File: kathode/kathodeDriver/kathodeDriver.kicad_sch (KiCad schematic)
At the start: 226 parts, among them J1 Conn_01x04, J2 Conn_01x02, Q1 Q_NPN_BEC, Q10 Q_NPN_BEC, Q11 Q_NPN_BEC, Q12 Q_NPN_BEC, Q13 Q_NPN_BEC, Q14 Q_NPN_BEC, Q15 Q_NPN_BEC, Q16 Q_NPN_BEC, Q17 Q_NPN_BEC, Q18 Q_NPN_BEC, Q19 Q_NPN_BEC, Q2 Q_NPN_BEC, Q20 Q_NPN_BEC, Q21 Q_NPN_BEC, Q22 Q_NPN_BEC, Q23 Q_NPN_BEC, Q24 Q_NPN_BEC, Q25 Q_NPN_BEC, Q26 Q_NPN_BEC, Q27 Q_NPN_BEC, Q28 Q_NPN_BEC, Q29 Q_NPN_BEC, Q3 Q_NPN_BEC, Q30 Q_NPN_BEC, Q31 Q_NPN_BEC, Q32 Q_NPN_BEC, Q33 Q_NPN_BEC, Q34 Q_NPN_BEC, Q35 Q_NPN_BEC, Q36 Q_NPN_BEC, Q37 Q_NPN_BEC, Q38 Q_NPN_BEC, Q39 Q_NPN_BEC, Q4 Q_NPN_BEC, Q40 Q_NPN_BEC, Q41 Q_NPN_BEC, Q42 Q_NPN_BEC, Q43 Q_NPN_BEC, Q44 Q_NPN_BEC, Q45 Q_NPN_BEC, Q46 Q_NPN_BEC, Q47 Q_NPN_BEC, Q48 Q_NPN_BEC, Q49 Q_NPN_BEC, Q5 Q_NPN_BEC, Q50 Q_NPN_BEC, Q51 Q_NPN_BEC, Q52 Q_NPN_BEC, Q53 Q_NPN_BEC, Q54 Q_NPN_BEC, Q55 Q_NPN_BEC, Q56 Q_NPN_BEC, Q57 Q_NPN_BEC, Q58 Q_NPN_BEC, Q59 Q_NPN_BEC, Q6 Q_NPN_BEC, Q60 Q_NPN_BEC, Q61 Q_NPN_BEC, Q62 Q_NPN_BEC, Q63 Q_NPN_BEC, Q64 Q_NPN_BEC, Q7 Q_NPN_BEC, Q8 Q_NPN_BEC, Q9 Q_NPN_BEC, U1 74AUP1G32, U10 4017, U11 4017, U2 4017, U3 4081, U4 4081, U5 4017, U6 4017, U7 4017, U8 4017, U9 4017

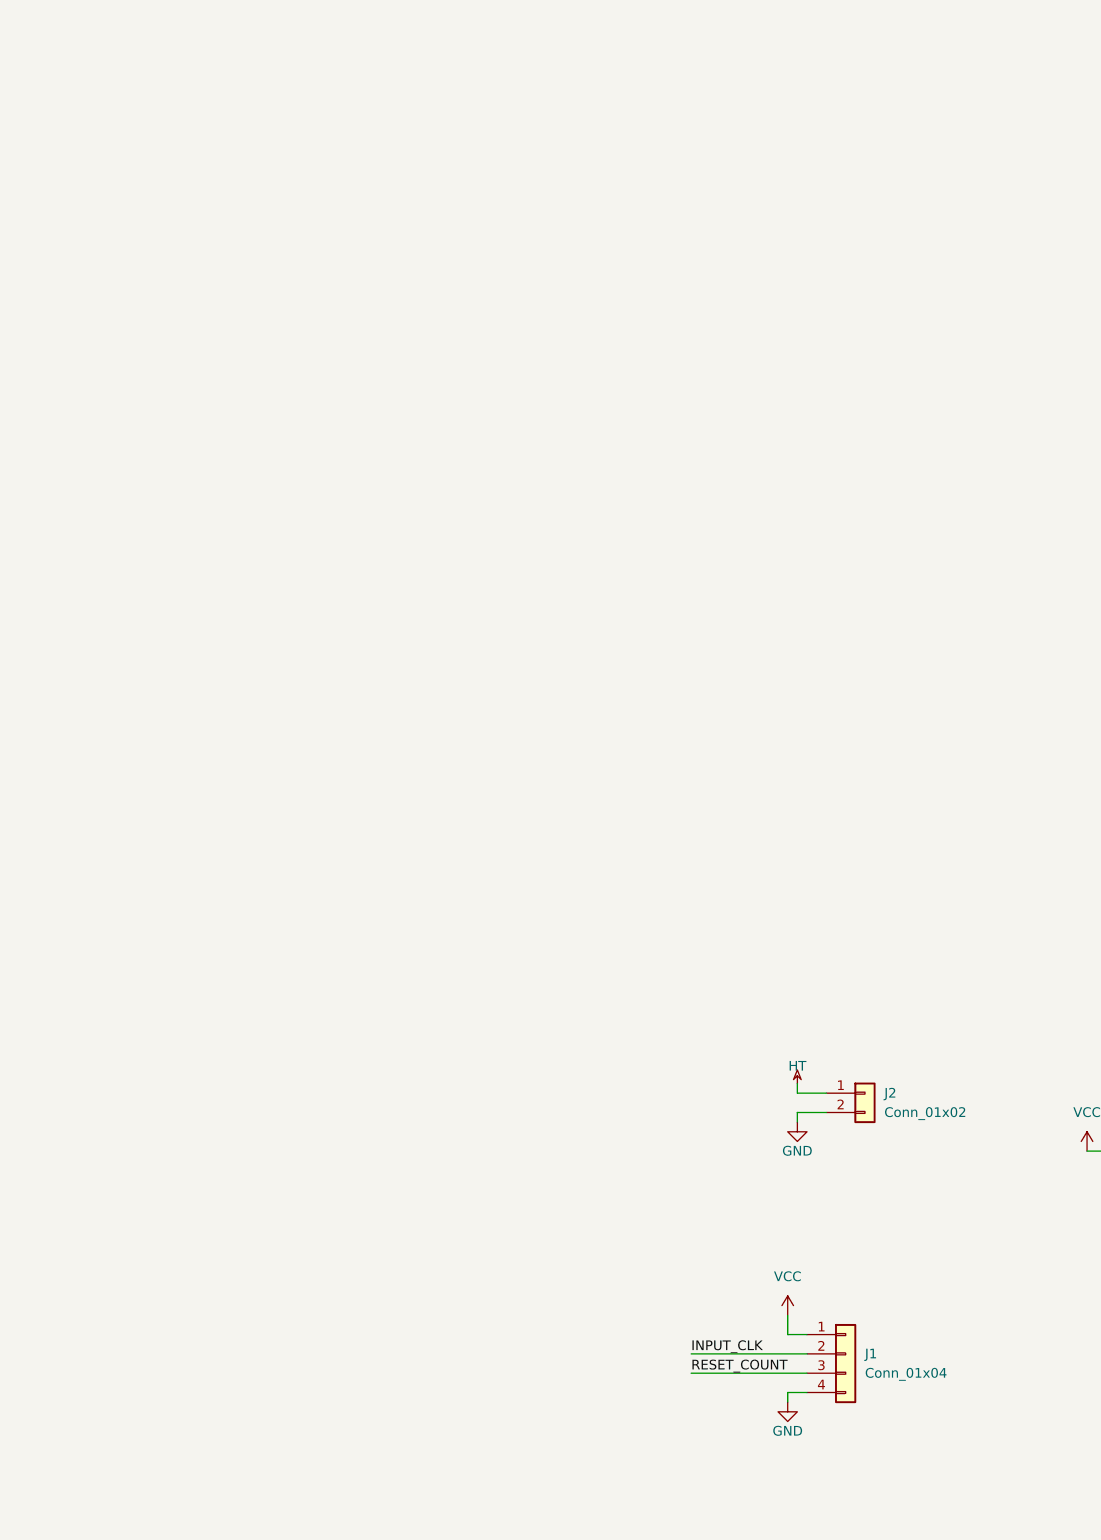
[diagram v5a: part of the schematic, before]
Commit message: Schematic of anode basically done, started layout
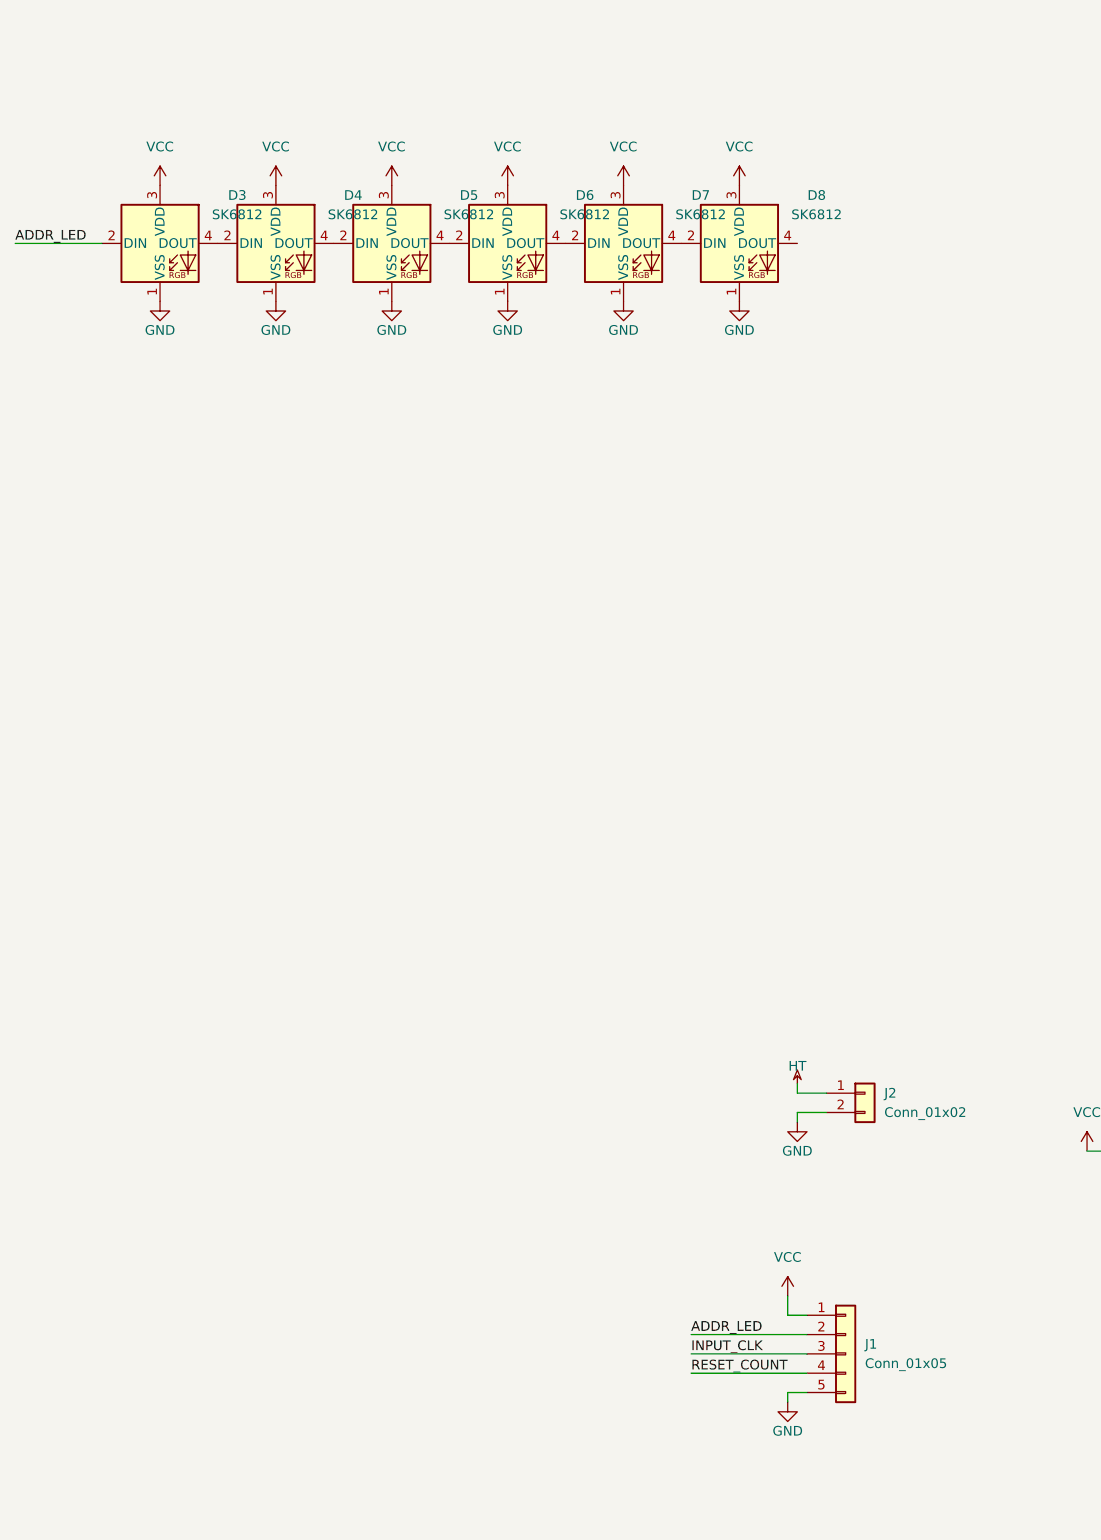
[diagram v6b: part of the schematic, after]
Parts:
- added D3, D4, D5, D6, D7, D8: SK6812, LED_SMD:LED_SK6812_PLCC4_5.0x5.0mm_P3.2mm, symbol LED:SK6812
- J1: value Conn_01x04 -> Conn_01x05; footprint Connector_JST:JST_XH_B4B-XH-AM_1x04_P2.50mm_Vertical -> Connector_JST:JST_XH_B4B-XH-AM_1x05_P2.50mm_Vertical; symbol Connector_Generic:Conn_01x04 -> Connector_Generic:Conn_01x05
- Q1, Q10, Q11, Q12, Q13, Q14, Q15, Q16, Q17, Q18, Q19, Q2, Q20, Q21, Q22, Q23, Q24, Q25, Q26, Q27, Q28, Q29, Q3, Q30, Q31, Q32, Q33, Q34, Q35, Q36, Q37, Q38, Q39, Q4, Q40, Q41, Q42, Q43, Q44, Q45, Q46, Q47, Q48, Q49, Q5, Q50, Q51, Q52, Q53, Q54, Q55, Q56, Q57, Q58, Q59, Q6, Q60, Q61, Q62, Q63, Q64, Q7, Q8, Q9: LCSC C151355 -> C20069141
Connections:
- net GND: now also J1.5 (Pin_5), D3.1 (VSS), D4.1 (VSS), D5.1 (VSS), D6.1 (VSS), D7.1 (VSS), D8.1 (VSS); no longer J1.4 (Pin_4)
- net INPUT_CLK: now also J1.3 (Pin_3); no longer J1.2 (Pin_2)
- net RESET_COUNT: now also J1.4 (Pin_4); no longer J1.3 (Pin_3)
- net VCC: now also D3.3 (VDD), D4.3 (VDD), D5.3 (VDD), D6.3 (VDD), D7.3 (VDD), D8.3 (VDD)
- new net: D4.4 (DOUT), D5.2 (DIN)
- new net: D5.4 (DOUT), D6.2 (DIN)
- new net: D6.4 (DOUT), D7.2 (DIN)
- new net: D7.4 (DOUT), D8.2 (DIN)
- new net: D3.4 (DOUT), D4.2 (DIN)
- new net ADDR_LED: D3.2 (DIN), J1.2 (Pin_2)
